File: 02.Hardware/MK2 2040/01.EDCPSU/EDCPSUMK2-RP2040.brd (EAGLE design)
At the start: 96 x 60.8 mm, 192 parts, among them IC1 W25Q64JVSSIQ, IC2 LM4040C25FTA, IC3 AP64501SP-13, J1 DX07S016JA1R1500, J2 RP2040TR7, J4 FTDI CONECTOR, J6 Display, K1 FLEX CONNECTORES, Q2 2N7002PW, Q4 2N7002PW, Q5 2N7002PW, Q9 2N7002PW, U10 IP2721, U2 MCP4725, U3 SN74AC14PWR, U4 MAX9938FEUK+T, U6 SN74AC14PWR, U7 TPIC2810D, U9 MAX9064EUK+T, Y1 ABLS-12.000MHZ-B4-T

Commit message: 1º Colocacion de componentes en el brd
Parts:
- removed R38: N.C, SparkFun-Resistors:0805
- removed TP1, TP10, TP11, TP12, TP14, TP4, TP6, TP7, TP9: (no value), SparkFun-Connectors:1X01_POGOPIN_HOLE_LARGE
- removed TP2: VCCIO, SparkFun-Connectors:1X01_POGOPIN_HOLE_LARGE
- removed TP3: M01NOSILK-KIT, SparkFun-Connectors:1X01NS-KIT
- removed TP5: PEDAL, SparkFun-Connectors:1X01_POGOPIN_HOLE_LARGE
- added C65: N.C., SparkFun-Passives:0805
- added JP1, JP2, JP5: JUMPER-SMT_2_NO_NO-SILK, SparkFun-Jumpers:SMT-JUMPER_2_NO_NO-SILK
- added R58, R60: N.C, SparkFun-Resistors:0805
- C45, C46: device SparkFun-Passives:1206 -> SparkFun-Passives:0805
- Y1: value ABLS-12.000MHZ-B4-T -> ABM3C-12.000MHZ-D4Y-T; device ABLS-12.000MHZ-B4-T:ABLS -> ABM3C-12.000MHZ-D4Y-T:ABM3C16000MHZD4YT
- moved C59 512.2 mm to (92.0, 57.8), turned to 180 degrees
- moved C61 492.7 mm to (92.4, 50.6)
- moved C31 484.6 mm to (106.2, 52.1), flipped to the bottom
- moved C62 482.4 mm to (90.8, 65.7), turned to 90 degrees
- moved C63 466.7 mm to (90.8, 62.4), turned to 270 degrees
- moved C52 448.9 mm to (82.0, 58.7), turned to 180 degrees
- moved C3 444.7 mm to (89.0, 65.8), turned to 90 degrees
- moved C64 429.0 mm to (89.0, 62.4), turned to 270 degrees
- moved C8 426.9 mm to (97.4, 71.1), flipped to the bottom
- moved C4 405.3 mm to (82.7, 64.9), turned to 270 degrees
- moved C50 377.7 mm to (94.4, 46.5), turned to 90 degrees
- moved C7 367.5 mm to (102.4, 46.4), turned to 90 degrees
- moved C33 362.3 mm to (106.2, 52.5), turned to 180 degrees
- moved C6 342.0 mm to (98.8, 59.0), turned to 270 degrees
- moved C32 341.4 mm to (95.9, 46.5), turned to 90 degrees
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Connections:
- net SPARE renamed PDL
- removed net IN+1: D1.2
- removed net SPARE2: R38.1
- removed net VCC-ISO: C1.2, C12.2, C15.1, C16.2, C2.2, C20.2, C25.2, C26.1, C3.2, C31.2, C44.2, C45.1, C5.2, C50.2, C51.2, C52.2, C53.2, C57.1, C6.2, C60.2, C62.2, C7.2, C8.2, D2.2, D3.2, D7.2, IC1.8, J2.1, J2.10, J2.22, J2.33, J2.42, J2.44, J2.48, J2.49, J4.P$4, J6.2, K1.4, L1.2, LS1.3, R13.2, R15.1, R19.2, R35.1, R40.2, R52.2, R53.2, R54.2, R57.2, R66.1, U2.3, U3.14, U6.14, U7.1, U9.1, Z1.1
- removed net VCCIO: TP2.1
- new net 3V3MCU: C1.2, C12.2, C15.1, C16.2, C2.2, C20.2, C25.2, C26.1, C3.2, C31.2, C44.2, C45.1, C5.2, C50.2, C51.2, C52.2, C53.2, C57.1, C6.2, C60.2, C62.2, C7.2, C8.2, D2.2, D3.2, D7.2, IC1.8, J2.1, J2.10, J2.22, J2.33, J2.42, J2.44, J2.48, J2.49, J4.P$4, J6.2, K1.4, L1.2, LS1.1, R13.2, R15.1, R19.2, R35.1, R40.2, R52.2, R53.2, R54.2, R57.2, R66.1, U2.3, U3.14, U6.14, U7.1, U9.1, Z1.1
- new net N$45: R58.2, U2.5
- new net N$48: R60.2, U2.4
- net FB: now also JP2.2; no longer C52.1, R15.2, R16.1
- net GND: now also C65.1, Y1.2, Y1.4; no longer D4.3, TP12.1
- net GND_IN: now also D4.3
- net IN+: now also D1.2
- net ISENSE: no longer TP4.1
- net N$19: now also C65.2
- net N$38: now also C52.1, JP2.1, R15.2, R16.1; no longer R38.2, TP1.1
- net N$63: now also Y1.3; no longer Y1.2
- net OVC_ALARM: no longer TP10.1
- net PEDAL: no longer TP5.1
- net PUSH: no longer TP9.1
- net SCL: now also R58.1; no longer TP7.1, U2.5
- net SDA: now also R60.1; no longer TP6.1, U2.4
- net USB_D+: now also JP5.2
- net USB_D-: now also JP1.2
- net USB_DM: now also JP1.1
- net USB_DP: now also JP5.1
- net VOSEN: no longer TP3.1
- net VOUT: no longer TP11.1
- net VO_TPS: no longer TP14.1
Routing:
- net 3V3MCU: track 0.00 -> 124.9 mm, vias 0 -> 17
- net VCC-ISO: track 92.8 -> 0.00 mm, vias 13 -> 0
- net ISENSE: track 97.6 -> 37.0 mm, vias 4 -> 1
- net SDA: track 74.3 -> 17.3 mm, vias 3 -> 0
- net MOSI: track 76.0 -> 21.4 mm, vias 2 -> 1
- net SCL: track 69.1 -> 15.9 mm, vias 4 -> 0
- net VBUS_SENSE: track 108.2 -> 71.0 mm, vias 2 -> 1
- net GND: track 167.5 -> 196.1 mm, vias 144 -> 148
- net N$31: track 41.7 -> 17.1 mm
- net N$32: track 38.6 -> 15.0 mm
- net TX-O: track 21.8 -> 0.00 mm, vias 2 -> 0
- net EN_DCDC: track 99.1 -> 77.4 mm, vias 2 -> 1
- net RX-I: track 18.5 -> 0.00 mm, vias 2 -> 0
- net SS: track 47.5 -> 30.7 mm, vias 2 -> 1
- net PUSH_FILT: track 42.1 -> 25.6 mm, vias 2 -> 1
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- added copper zone on layer 15, net 3V3MCU
- removed copper zone on layer 15, net VCC-ISO

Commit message: Pequeños cambios
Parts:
- removed IC1: W25Q64JVSSIQ, W25Q64JVSSIQ:SOIC127P790X216-8N
- removed Z1: MMSZ5227B-7-F, MMSZ5227B-7-F:SOD3716X135N
- added C66: 100n 50v X7R/X5R, SparkFun-Passives:0805
- added DZ1: MMSZ5227B-7-F, MMSZ5227B-7-F:SOD3716X135N
- added U5: W25Q64JVSSIQ, W25Q64JVSSIQ:SOIC127P790X216-8N
- moved C28 9.94 mm to (13.7, 58.4), flipped to the bottom
- moved R57 5.62 mm to (109.0, 43.4)
- moved C21 3.83 mm to (16.5, 58.2)
- moved C61 2.35 mm to (90.1, 50.4)
- moved C17 1.64 mm to (19.4, 58.2)
- moved R46 1.57 mm to (92.9, 50.4)
- moved C18 1.56 mm to (22.4, 58.1)
- moved C10 1.11 mm to (19.4, 53.8), turned to 0 degrees
- moved L1 0.38 mm to (85.2, 69.4), turned to 0 degrees
- renumbered IC2 to U8, IC3 to U12, J2 to U1, PS1 to U11, Y1 to X1
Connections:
- net VCCA renamed 1V1MCU
- new net VCC-ISO: C6.2, U1.10
- net 2V5_REF: now also C66.2
- net 3V3MCU: now also DZ1.1, U5.8; no longer C6.2, IC1.8, U1.10, Z1.1
- net GND: now also C66.1, DZ1.2, U5.4; no longer IC1.4, Z1.2
- net QSPI_SCLK: now also U5.6; no longer IC1.6
- net QSPI_SD0: now also U5.2; no longer IC1.2
- net QSPI_SD1: now also U5.5; no longer IC1.5
- net QSPI_SD2: now also U5.3; no longer IC1.3
- net QSPI_SD3: now also U5.7; no longer IC1.7
- net QSPI_SS: now also U5.1; no longer IC1.1
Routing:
- net 2V5_REF: track 5.68 -> 22.5 mm
- net VCC: track 41.0 -> 34.1 mm
- net GND: track 196.1 -> 192.1 mm
- net 3V3MCU: track 124.9 -> 122.3 mm
- net XOUT: track 6.77 -> 5.01 mm
- net VCC-ISO: track 0.00 -> 1.60 mm
- net ROTA_FILT: track 3.12 -> 4.13 mm

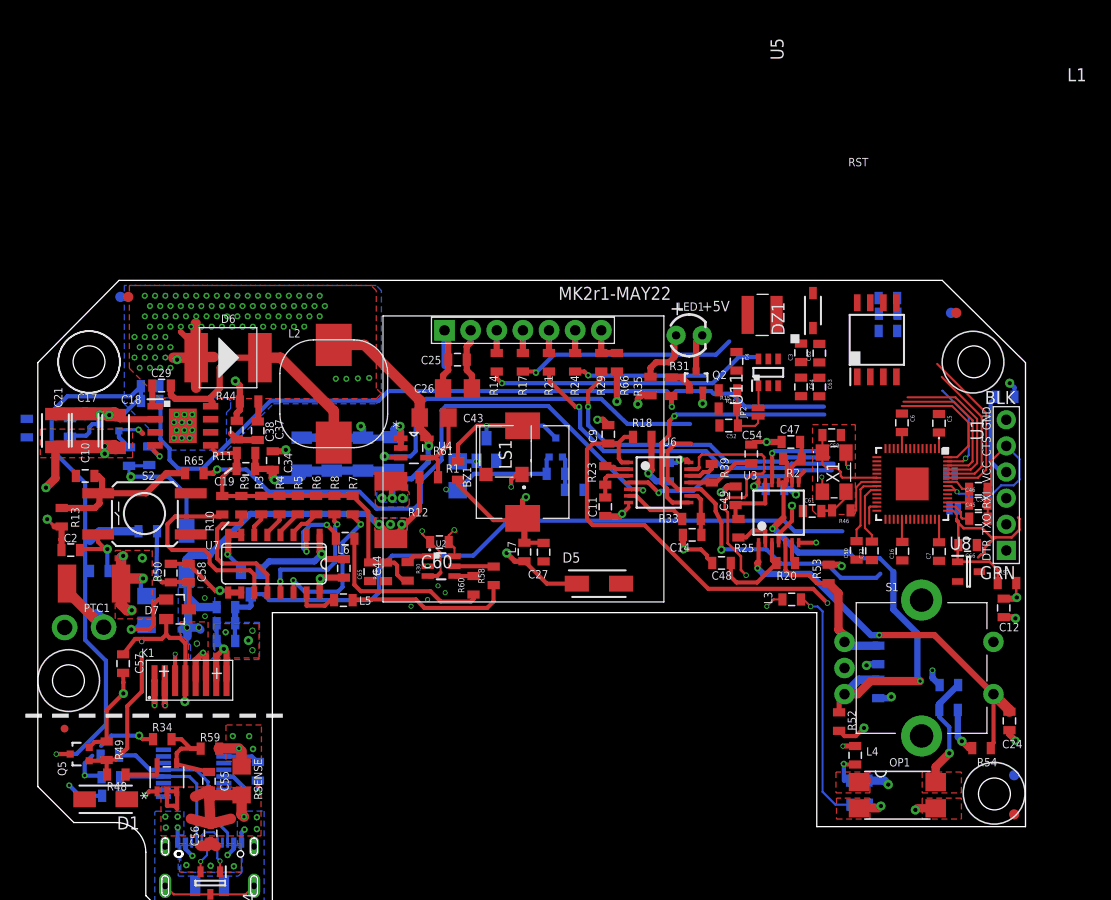
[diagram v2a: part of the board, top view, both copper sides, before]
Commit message: Continuacion de cambios. Rutado inicial de todos los componentes. Falta asignacion de pines.
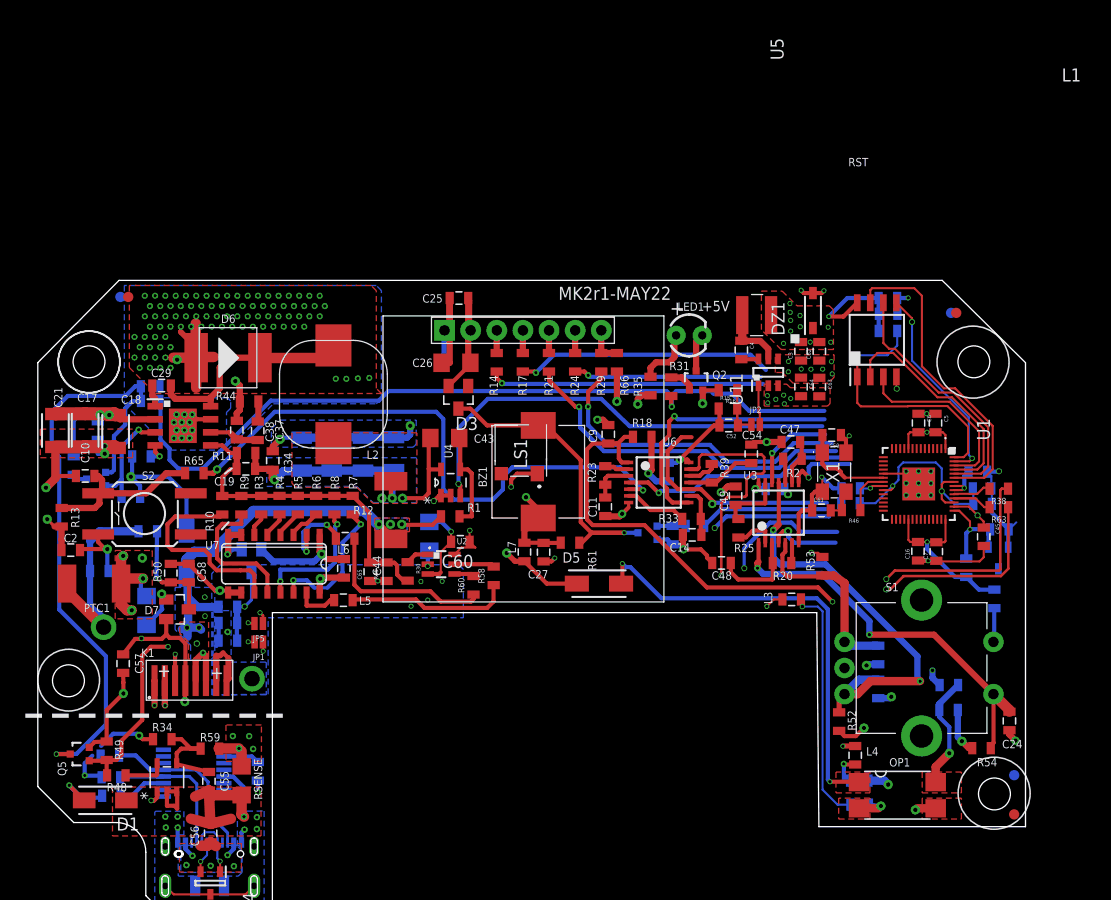
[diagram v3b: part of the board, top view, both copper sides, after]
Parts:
- removed C1: 100n 50v X7R/X5R, SparkFun-Passives:0805
- removed IN-: TEST-POINT3, SparkFun-Connectors:PAD.03X.03
- removed J4: FTDI CONECTOR, SparkFun-Connectors:FTDI_DEVICE_SIDE
- added R38: 27R, SparkFun-Resistors:0805
- added R63: R27, SparkFun-Resistors:0805
- moved JP5 68.8 mm to (36.3, 39.5), flipped to the top, turned to 180 degrees
- moved JP1 68.8 mm to (36.3, 37.6), flipped to the top, turned to 180 degrees
- moved R61 12.9 mm to (66.5, 47.3), turned to 180 degrees
- moved R32 12.8 mm to (76.5, 48.0), turned to 270 degrees
- moved R28 12.2 mm to (78.7, 48.9)
- moved Q9 12.2 mm to (74.1, 48.3), turned to 270 degrees
- moved C28 6.91 mm to (20.6, 58.2)
- moved C51 6.49 mm to (52.9, 47.9)
- moved C50 6.07 mm to (93.8, 52.6), flipped to the bottom, turned to 180 degrees
- moved C25 5.99 mm to (55.7, 71.1)
- moved D3 5.76 mm to (55.7, 61.4), flipped to the top, turned to 180 degrees
- moved Q4 5.49 mm to (20.5, 53.5)
- moved C32 5.08 mm to (93.8, 51.1), flipped to the bottom, turned to 180 degrees
- moved U4 4.90 mm to (54.9, 53.2), turned to 90 degrees
- moved R1 4.34 mm to (54.9, 49.9)
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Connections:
- removed net DTR: J4.P$1
- removed net RX-I: J4.P$3
- removed net TX-O: J4.P$2
- removed net VCC-ISO: C6.2, U1.10
- new net N$64: JP5.1, R38.1
- new net N$65: JP1.1, R63.1
- net 3V3MCU: now also C6.2, U1.10; no longer C1.2, J4.P$4
- net GND: no longer C1.1, D1.1, J4.P$5, J4.P$6
- net GND_IN: now also D1.1; no longer IN-.P$1
- net USB_DM: now also R63.2; no longer JP1.1
- net USB_DP: now also R38.2; no longer JP5.1
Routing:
- net N$65: track 0.00 -> 84.9 mm, vias 0 -> 2
- net N$64: track 0.00 -> 83.6 mm, vias 0 -> 2
- net N$16: track 0.00 -> 43.5 mm, vias 0 -> 2
- net GND: track 192.1 -> 225.7 mm, vias 148 -> 165
- net 3V3MCU: track 122.3 -> 149.4 mm, vias 17 -> 30
- net USB_D+: track 7.34 -> 29.4 mm, vias 1 -> 2
- net USB_D-: track 9.61 -> 29.5 mm, vias 1 -> 2
- net QSPI_SD3: track 16.3 -> 31.1 mm
- net QSPI_SS: track 11.9 -> 26.2 mm, vias 0 -> 1
- net N$31: track 17.1 -> 30.8 mm
- net BUZZ: track 0.00 -> 12.8 mm
- net 2V5_REF: track 22.5 -> 9.82 mm, vias 0 -> 1
- net VO_TPS: track 43.0 -> 31.5 mm, vias 5 -> 4
- net 1V1MCU: track 12.1 -> 23.2 mm, vias 0 -> 2
- net QSPI_SCLK: track 13.9 -> 24.9 mm
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- added copper zone on layer 1, net 3V3MCU
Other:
- outline, holes or cut-outs redrawn

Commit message: Pequeñas modificaciones
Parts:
- R63: value R27 -> 27R
- moved D6 1.34 mm to (33.2, 66.6)
- moved R66 0.24 mm to (71.3, 64.8)
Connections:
- new net VCC-ISO: C15.1, C8.2, U5.8
- net 3V3MCU: no longer C15.1, C8.2, U5.8
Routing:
- net VCC-ISO: track 0.00 -> 10.4 mm, vias 0 -> 1
- net 3V3MCU: track 149.4 -> 139.0 mm, vias 30 -> 29
- net GND: track 225.7 -> 219.1 mm
- net N$51: track 21.8 -> 23.1 mm
- net VO_TPS: vias 4 -> 10

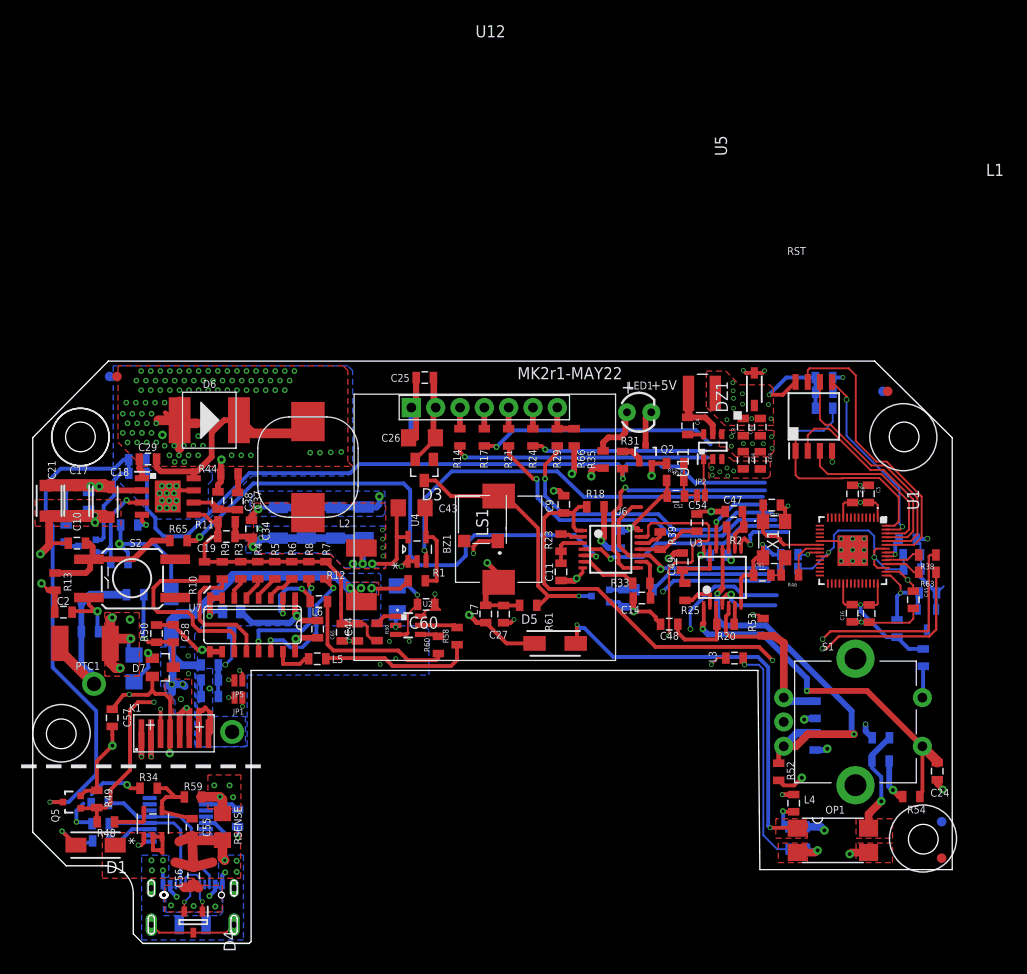
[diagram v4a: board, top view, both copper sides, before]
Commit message: Propuesta de routeado 1
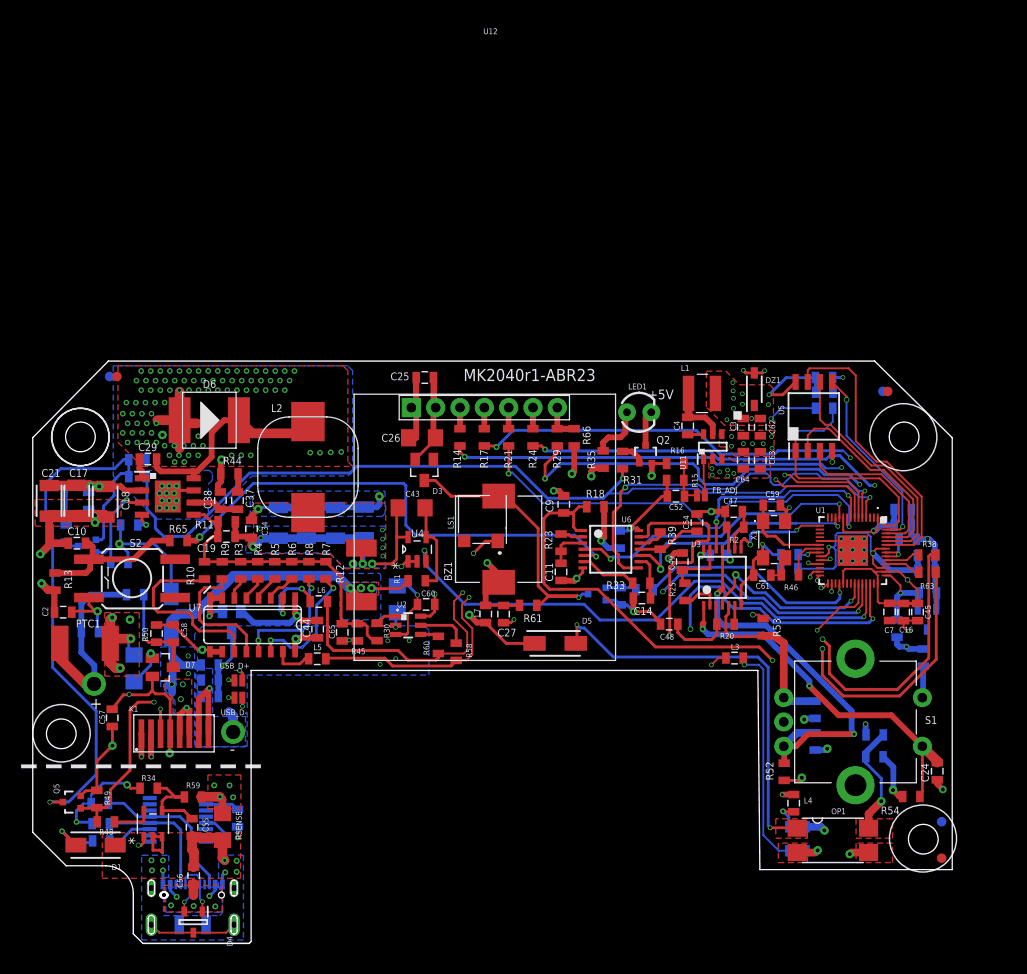
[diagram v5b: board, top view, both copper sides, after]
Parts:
- removed IN+: TEST-POINT3, SparkFun-Connectors:PAD.03X.03
- removed JP1, JP5: JUMPER-SMT_2_NO_NO-SILK, SparkFun-Jumpers:SMT-JUMPER_2_NO_NO-SILK
- added USB_D+, USB_D-: JUMPER-SMT_2_NO_NO-SILK, SparkFun-Jumpers:SMT-JUMPER_2_NO_NO-SILK
- moved C6 5.48 mm to (105.6, 57.3), flipped to the bottom, turned to 0 degrees
- moved C16 5.38 mm to (105.7, 46.6)
- moved C5 4.86 mm to (105.6, 55.7), flipped to the bottom, turned to 0 degrees
- moved C7 2.14 mm to (104.3, 46.6)
- moved R58 1.63 mm to (59.0, 42.5)
- moved C46 1.49 mm to (108.1, 51.0)
- moved C33 1.49 mm to (108.1, 52.5)
- moved C45 1.35 mm to (107.2, 46.6)
- moved R19 0.78 mm to (102.7, 31.5)
- moved R99 0.71 mm to (102.7, 33.8)
- moved R52 0.57 mm to (93.3, 29.9)
- moved Q9 0.42 mm to (73.7, 48.5)
- moved R32 0.42 mm to (76.1, 48.2)
- moved R27 0.36 mm to (25.7, 60.7)
- moved C38 0.25 mm to (34.4, 58.2)
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- renumbered JP2 to FB_ADJ
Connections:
- net N$72 renamed TX
- net N$73 renamed RX
- removed net N$24: U1.41
- removed net N$27: U1.40
- removed net N$30: U1.37
- removed net N$33: U1.39
- removed net N$36: U1.38
- removed net N$42: U1.36
- removed net N$57: U1.32
- removed net N$61: U1.30
- removed net N$62: U1.29
- removed net N$74: U1.4
- removed net N$75: U1.5
- removed net N$76: U1.6
- removed net N$77: U1.7
- removed net N$78: U1.8
- removed net N$79: U1.9
- removed net N$80: U1.11
- removed net N$81: U1.12
- removed net N$84: U1.15
- removed net N$88: U1.28
- removed net N$89: U1.27
- net BUZZ: now also U1.32
- net DSP_RST: now also U1.9
- net EN_DCDC: now also U1.4
- net IN+: no longer IN+.P$1
- net ISENSE: now also U1.39
- net MISO: now also U1.27
- net MOSI: now also U1.30
- net N$64: now also USB_D+.1; no longer JP5.1
- net N$65: now also USB_D-.1; no longer JP1.1
- net OVC_ALARM: now also U1.12
- net PEDAL_IP: now also U1.11
- net PUSH_FILT: now also U1.5
- net ROTA_FILT: now also U1.36
- net ROTB_FILT: now also U1.15
- net RPUSH_FILT: now also U1.8
- net SCK: now also U1.29
- net SCL: now also U1.7
- net SDA: now also U1.6
- net SEL: now also U1.37
- net SS: now also U1.28
- net USB_D+: now also USB_D+.2; no longer JP5.2
- net USB_D-: now also USB_D-.2; no longer JP1.2
- net VBUS_SENSE: now also U1.38
- net VOSEN: now also U1.40
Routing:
- net SDA: track 17.3 -> 86.5 mm, vias 0 -> 2
- net SCL: track 15.9 -> 82.1 mm, vias 0 -> 2
- net MOSI: track 25.0 -> 63.8 mm, vias 1 -> 3
- net SCK: track 26.8 -> 64.8 mm, vias 1 -> 3
- net MISO: track 18.2 -> 55.6 mm, vias 1 -> 3
- net SS: track 31.6 -> 60.1 mm, vias 1 -> 3
- net PUSH_FILT: track 25.7 -> 41.8 mm, vias 1 -> 2
- net VOSEN: track 72.1 -> 87.2 mm, vias 2 -> 3
- net EN_DCDC: track 77.7 -> 92.0 mm, vias 1 -> 2
- net VBUS_SENSE: track 78.5 -> 92.7 mm, vias 2 -> 3
- net ISENSE: track 44.2 -> 57.8 mm, vias 1 -> 2
- net RPUSH_FILT: track 8.77 -> 21.8 mm, vias 1 -> 2
- net DSP_RST: track 34.1 -> 46.9 mm, vias 1 -> 2
- net ROTA_FILT: track 7.18 -> 19.5 mm, vias 1 -> 2
- net SEL: track 71.6 -> 83.8 mm, vias 3 -> 4
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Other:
- board text added: "-"
- board text added: "MK2040r1-ABR23"
- board text removed: "ISEN"
- board text removed: "ISENSE"
- board text removed: "MK2r1-MAY22"
- board text removed: "OVC_ALARM"
- board text removed: "PEDAL"
- board text removed: "PUSH"
- board text removed: "RST"
- board text removed: "SCL"
- board text removed: "SDA"
- board text removed: "SPARE2"
- board text removed: "VOSEN"

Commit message: Propuesta de routeado 2
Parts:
- added JP1: 20021521-00010T1LF, 20021521-00010T1LF:20021521-00010T1LF
- moved C33 7.92 mm to (101.5, 48.0), turned to 180 degrees
- moved C66 7.39 mm to (105.8, 41.6), turned to 270 degrees
- moved C46 6.72 mm to (101.5, 50.0), turned to 0 degrees
- moved C12 5.73 mm to (103.8, 37.8), turned to 0 degrees
- moved C6 5.46 mm to (100.2, 56.8), turned to 270 degrees
- moved C5 4.18 mm to (101.6, 56.8), turned to 270 degrees
- moved U8 4.16 mm to (108.6, 41.7), turned to 180 degrees
- moved C31 3.98 mm to (103.2, 56.8), turned to 270 degrees
- moved R19 1.92 mm to (103.6, 33.2), turned to 90 degrees
- moved R57 1.50 mm to (106.5, 44.4), turned to 180 degrees
- moved L4 1.24 mm to (95.5, 26.7)
- moved R52 1.20 mm to (92.6, 28.9)
- moved R99 1.06 mm to (101.8, 33.2), turned to 90 degrees
- moved C16 0.60 mm to (105.7, 46.0)
- moved C45 0.60 mm to (107.2, 46.0)
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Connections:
- removed net N$100: U1.26
- new net RUN: JP1.10, U1.26
- new net SWO: JP1.6
- new net TDI: JP1.8
- net 3V3MCU: now also JP1.1
- net GND: now also JP1.3, JP1.5, JP1.7, JP1.9
- net SWCLK: now also JP1.4
- net SWDIO: now also JP1.2
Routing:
- net RUN: track 0.00 -> 19.0 mm, vias 0 -> 2
- net SWDIO: track 1.25 -> 13.0 mm
- net 3V3MCU: track 150.9 -> 159.6 mm
- net SWCLK: track 1.13 -> 9.79 mm
- net 2V5_REF: track 9.77 -> 16.7 mm
- net 1V1MCU: track 27.0 -> 20.4 mm
- net ROTB: track 41.5 -> 45.4 mm
- net MISO: track 55.6 -> 58.9 mm
- net DSP_RST: track 46.9 -> 44.8 mm
- net SCK: track 64.8 -> 66.8 mm
- net PEDAL-: track 90.6 -> 92.5 mm
- net SS: track 60.1 -> 61.7 mm
- net N$64: track 91.3 -> 92.5 mm
- net MOSI: track 63.8 -> 65.0 mm
- net N$65: track 92.4 -> 91.3 mm
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- added copper zone on layer 1, net N$16
- removed copper zone on layer 1, net VCCIO
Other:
- outline, holes or cut-outs redrawn
- board text added: "MK2-RP2040 v1-March-2023"
- board text added: "VIN"
- board text removed: "#SER:"
- board text removed: "+5V"
- board text removed: "12V"
- board text removed: "MK2040r1-ABR23"
- board text removed: "VOUT"
- board text removed: "V_TPS"

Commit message: Cambios menores antes de pedir a PCBWAY
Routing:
- net GND: track 213.5 -> 220.8 mm
- net GND_IN: track 43.1 -> 47.9 mm
- net IN+: track 31.7 -> 34.7 mm, vias 8 -> 11
